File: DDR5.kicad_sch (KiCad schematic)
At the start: 2 parts, among them U12 Bus_DDR5_DDR504111002KQ

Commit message: [#80386] Add company name in board settings
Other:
- company: Antmicro Ltd. -> Antmicro
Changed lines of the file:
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@@
 		(date "2023-07-27")
 		(rev "1.0.1")
-		(company "Antmicro Ltd.")
+		(company "Antmicro")
 		(comment 1 "www.antmicro.com")
-		(comment 2 "Antmicro Ltd")
 	)
 	(text "DDR5 RDIMM connector"

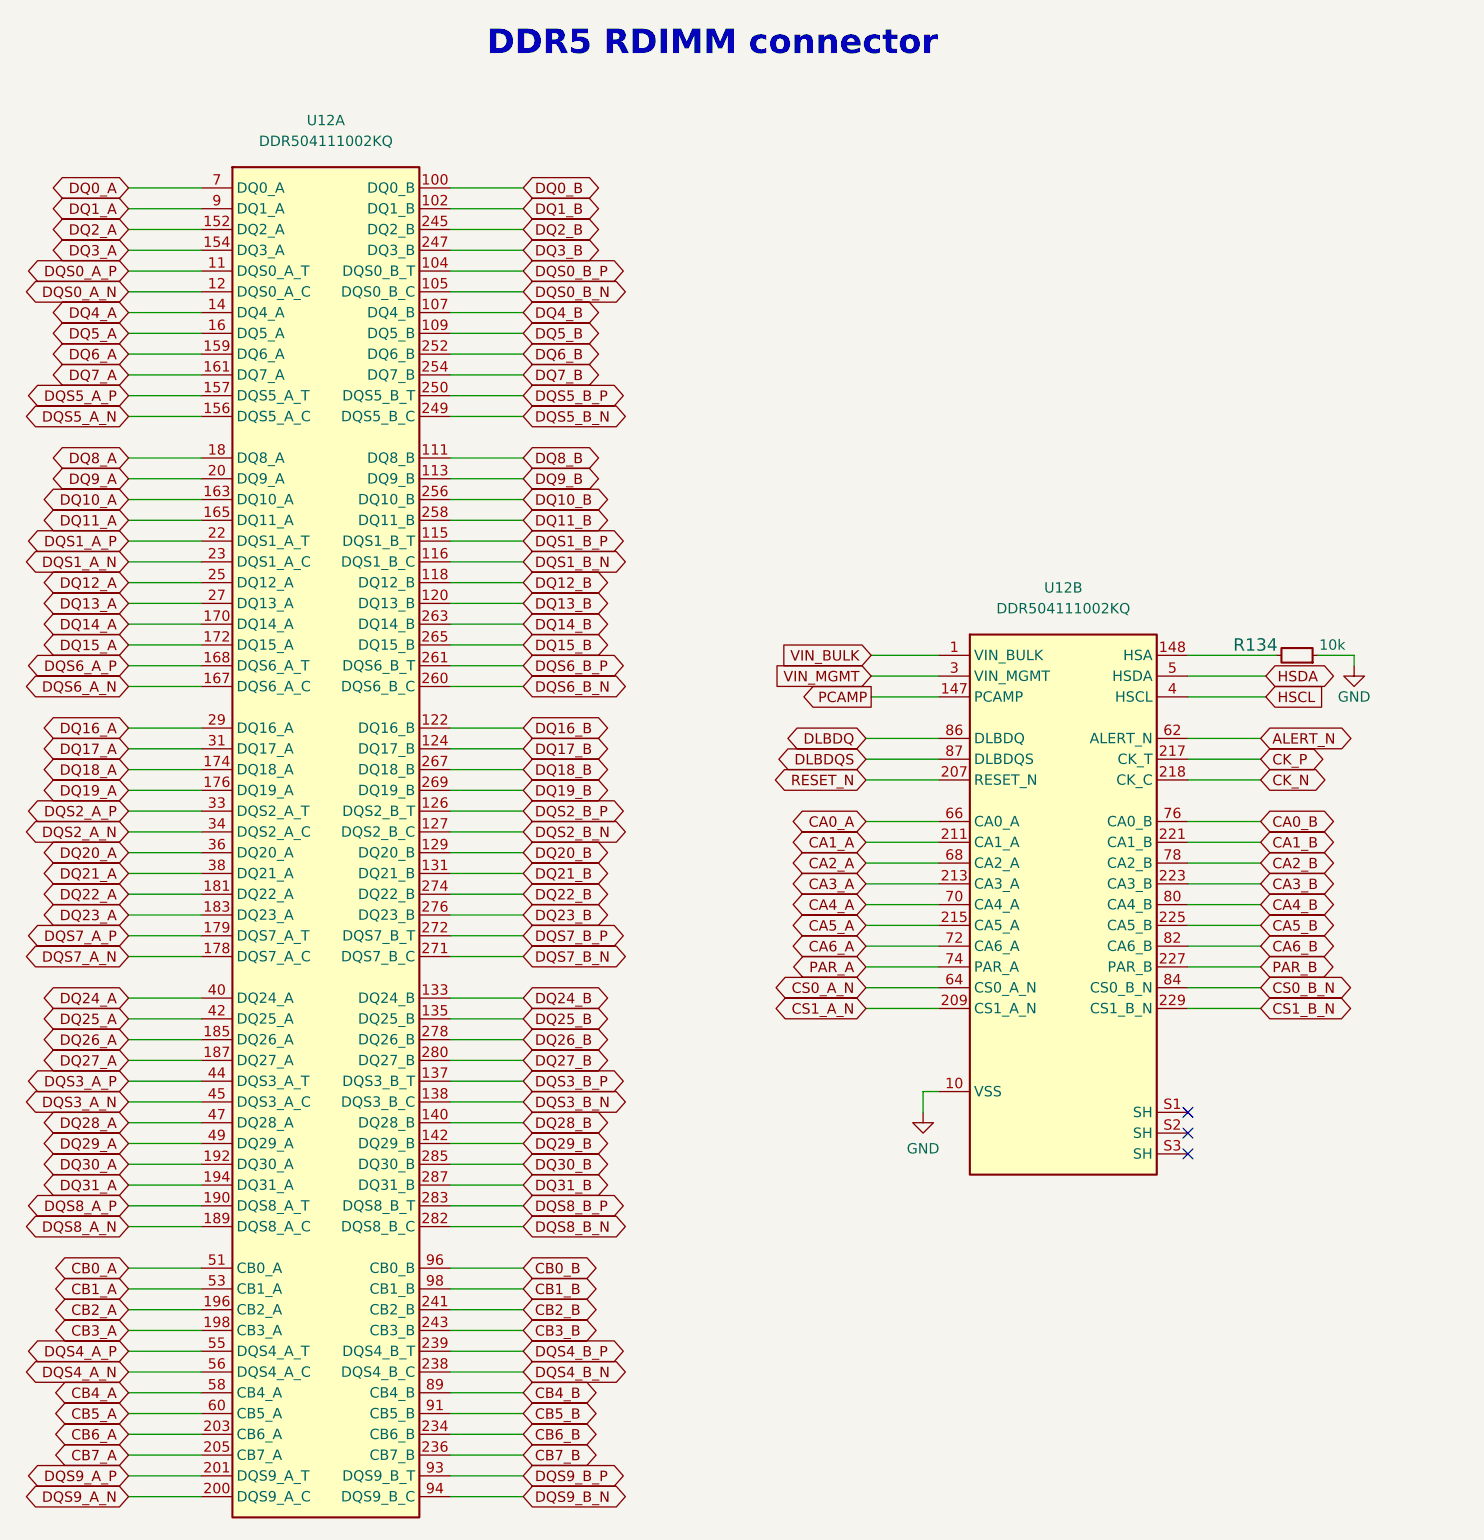
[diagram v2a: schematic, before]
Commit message: [#87036] Update components, clear DRC and ERC
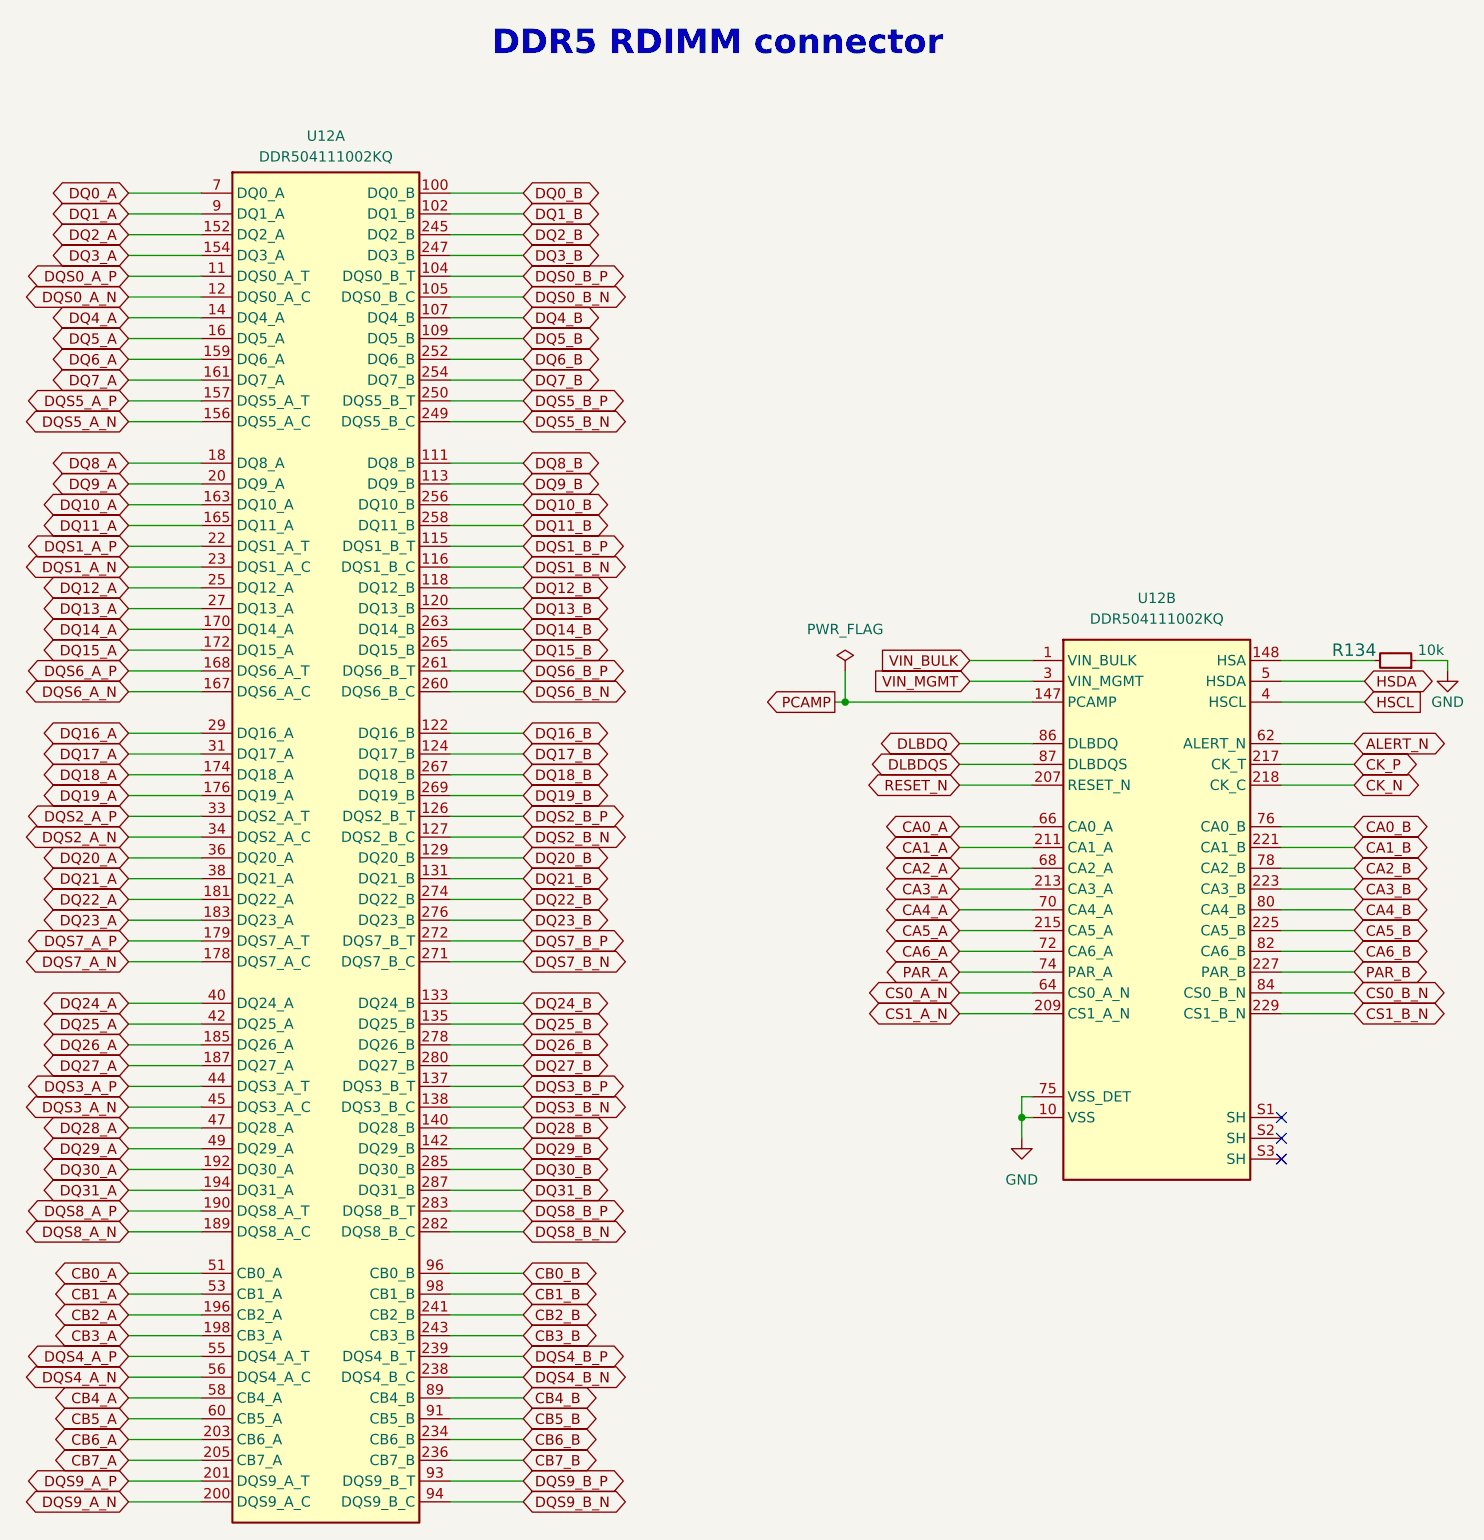
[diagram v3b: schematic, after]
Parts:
- R134: footprint data-center-rdimm-ddr5-tester-footprints:R_0402_1005Metric -> antmicro-footprints:R_0402_1005Metric; symbol data-center-rdimm-ddr5-tester:R_10k_0402 -> antmicroResistors0402:R_10k_0402
- U12: footprint data-center-rdimm-ddr5-tester-footprints:Bus_DDR5_Socket_Amphenol_DDR504111002KQ -> antmicro-footprints:Bus_DDR5_Socket_Amphenol_DDR504111002KQ; symbol data-center-rdimm-ddr5-tester:Bus_DDR5_DDR504111002KQ -> antmicroMemoryConnectorsPCCardSockets:Bus_DDR5_DDR504111002KQ
- U12: footprint data-center-rdimm-ddr5-tester-footprints:Bus_DDR5_Socket_Amphenol_DDR504111002KQ -> antmicro-footprints:Bus_DDR5_Socket_Amphenol_DDR504111002KQ; symbol data-center-rdimm-ddr5-tester:Bus_DDR5_DDR504111002KQ -> antmicroMemoryConnectorsPCCardSockets:Bus_DDR5_DDR504111002KQ_CUSTOM_1xDetectPin
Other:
- moved on the sheet: R134, U12A
